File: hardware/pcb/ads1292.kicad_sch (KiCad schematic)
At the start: 36 parts, among them J5 ECG pads, U8 ADS1292RIRSMT

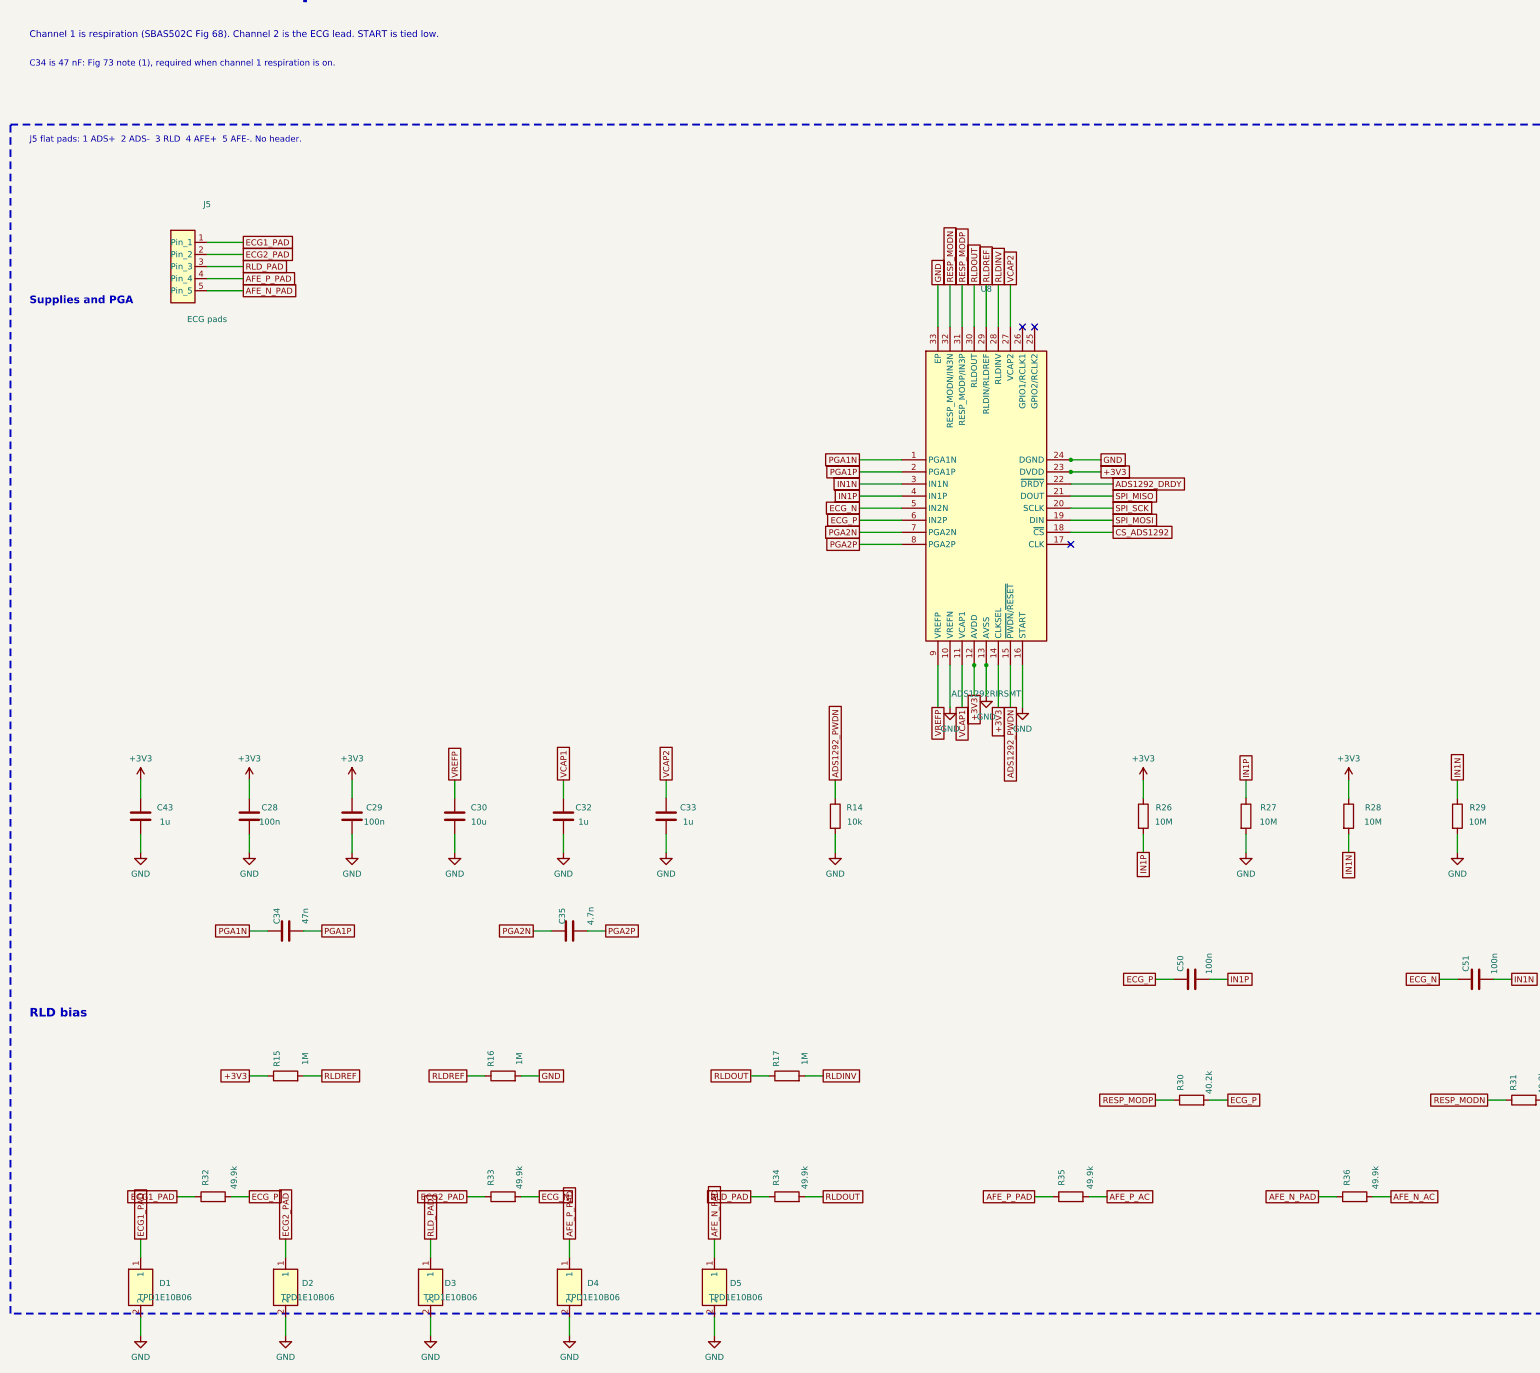
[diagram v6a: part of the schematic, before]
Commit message: Add defibrillator clamps and a charge-temperature cut-off.
Series electrode resistors are now DPCR2512 51k pulse parts, with an S30-A90X gas discharge tube on each patient pad ahead of the existing TPD1E10B06. The MCP73831 stays; a PicoStar FET floats PROG until firmware enables charge, and a 3-pin cell pad feeds a 10k NTC into GPIO39.

Co-authored-by: Riyu-D1 <Riyu-D1@users.noreply.github.com>
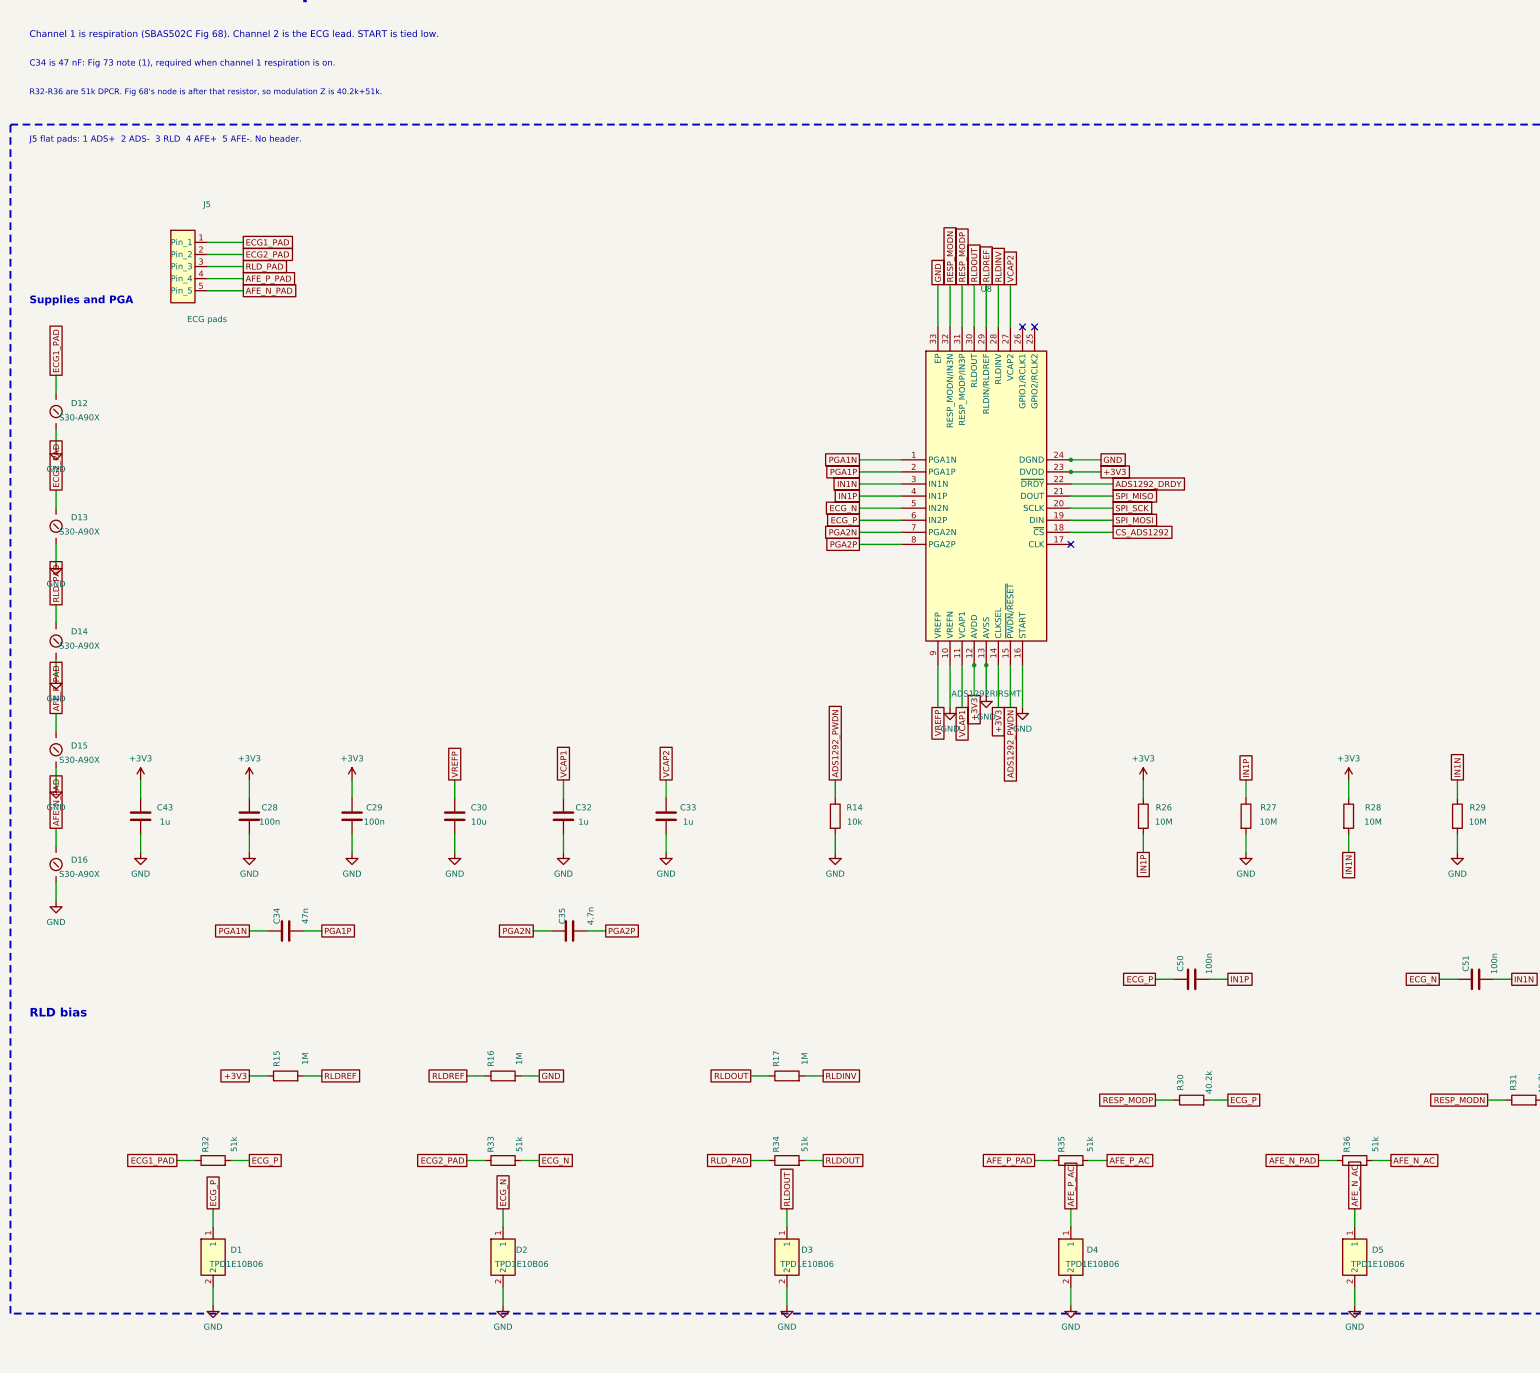
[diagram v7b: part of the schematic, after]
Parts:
- added D12, D13, D14, D15, D16: S30-A90X, vitalq:GDT_S30, symbol vitalq:GDT
- R32, R33, R34, R35, R36: value 49.9k -> 51k; footprint Resistor_SMD:R_0402_1005Metric -> Resistor_SMD:R_2512_6332Metric
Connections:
- net AFE_N_AC: now also D5.1
- net AFE_N_PAD: now also D16.1; no longer D5.1
- net AFE_P_AC: now also D4.1
- net AFE_P_PAD: now also D15.1; no longer D4.1
- net ECG1_PAD: now also D12.1; no longer D1.1
- net ECG2_PAD: now also D13.1; no longer D2.1
- net ECG_N: now also D2.1
- net ECG_P: now also D1.1
- net GND: now also D12.2, D13.2, D14.2, D15.2, D16.2
- net RLDOUT: now also D3.1
- net RLD_PAD: now also D14.1; no longer D3.1
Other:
- note added: "R32-R36 are 51k DPCR. Fig 68's node is after that resistor, so modulation Z is 40.2k+51k."
